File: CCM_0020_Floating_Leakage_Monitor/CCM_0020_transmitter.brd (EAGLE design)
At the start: 76.2 x 76.2 mm, 61 parts, among them IC1 LMC6041, IC2 LT1494, IC3 LT1495, IC4 LTC1440, IC6 LT6656A-5.0V, Q1 SMP4117A, Q2 SMP4117A, Q3 SMP4117A, Q4 SMP4117A, T1 3904SM

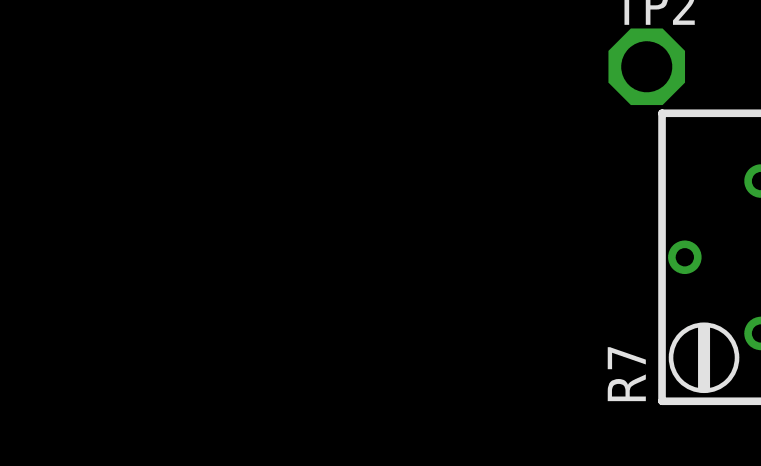
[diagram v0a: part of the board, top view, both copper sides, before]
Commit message: CCM_0020 directory organization
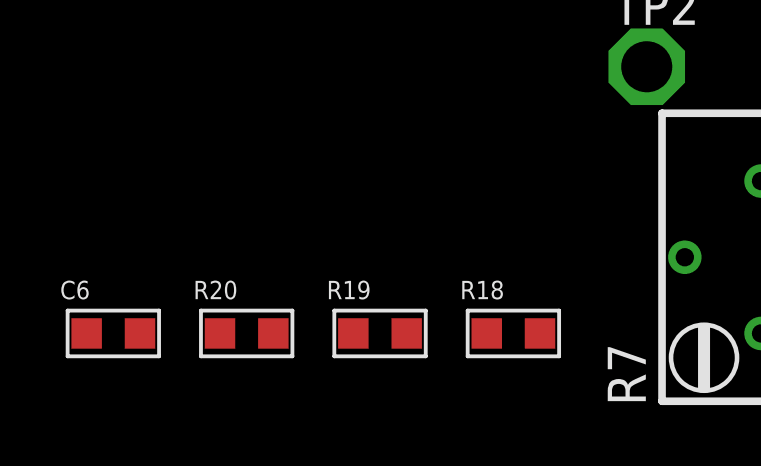
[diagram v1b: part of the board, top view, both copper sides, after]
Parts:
- added C6: 0.1u, acrooptics:0603
- added R18: 0, acrooptics:0603
- added R19: 360k, acrooptics:0603
- added R20: 4.3k, acrooptics:0603
- C5: value 0.05u -> 50n
- R11: value 20M -> 10M
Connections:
- removed net N$17: D11.C, IC3.5, R15.2
- removed net N$21: R8.1
- new net N$2: IC4.5, R18.1, R19.2
- new net N$5: C6.2, R20.1
- net GND: now also C6.1, R19.1
- net VREF: now also D11.C, IC3.5, R15.2, R18.2, R20.2, R8.1; no longer IC4.5
